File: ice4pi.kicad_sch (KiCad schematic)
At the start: 25 parts, among them J1 Conn_02x03, J2 Raspberry_Pi_2_3, J3 USB_C_Receptacle_USB2.0, J4 RJ45_Amphenol_RJMG1BD3B8K1ANR, U1 ENC28J60x-SS, U2 DSC1001DE1-025.0000

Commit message: feat: poe
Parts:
- removed C1, C2: 100 nF, Capacitor_SMD:C_0402_1005Metric, symbol Device:C
- removed J4: RJ45_Amphenol_RJMG1BD3B8K1ANR, Connector_RJ:RJ45_Amphenol_RJMG1BD3B8K1ANR, symbol Connector:RJ45_Amphenol_RJMG1BD3B8K1ANR
- removed L1: L, Inductor_SMD:L_1210_3225Metric, symbol Device:L
- removed R1, R2, R3, R4: 50, Resistor_SMD:R_0402_1005Metric, symbol Device:R
- removed R6, R7: 1K, Resistor_SMD:R_0402_1005Metric, symbol Device:R
- added C10, C9: 100 nF, Capacitor_SMD:C_0402_1005Metric, symbol Device:C
- added J5: RJ45_Abracon_ARJP11A-MASA-B-A-EMU2, Connector_RJ:RJ45_Abracon_ARJP11A-MA_Horizontal, symbol Connector:RJ45_Abracon_ARJP11A-MASA-B-A-EMU2
- added L2: L, Inductor_SMD:L_1210_3225Metric, symbol Device:L
- added LSI-U1: lsi-powermodule-7, lsi:lsi-powermodule-7, symbol lsi:lsi-powermodule-7
- added R11, R12, R13, R14: 50, Resistor_SMD:R_0402_1005Metric, symbol Device:R
- added R15, R16: 1K, Resistor_SMD:R_0402_1005Metric, symbol Device:R
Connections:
- net +3.3V: now also L2.1
- net +5V: now also LSI-U1.3 (VPP_OUT)
- net GND: now also C10.2, C9.2, J5.12, J5.14, J5.SH, LSI-U1.4 (GND), LSI-U1.5 (S1)
- net LEDA: now also R15.1
- net LEDB: now also R16.1
- new net: C9.1, J5.4 (TCT), L2.2, R11.1, R12.1
- new net: C10.1, J5.5 (RCT), R13.1, R14.1
- new net: J5.6 (RD-), R14.2
- new net: J5.3 (RD+), R13.2
- new net: J5.1 (TD+), R11.2
- new net: J5.11, R15.2
- new net: J5.13, R16.2
- new net: J5.2 (TD-), R12.2
- new net POE_V+: J5.9 (V+), LSI-U1.2 (VPP_IN)
- new net POE_V-: J5.10 (V-), LSI-U1.1 (GND)
- no-connect marks 22 -> 23
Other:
- note removed: "2 to 1 jumper array."
- moved on the sheet: C5, C6, C7, C8, J1, J2, J3, R9

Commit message: feat: commit 2
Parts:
- removed R11, R12, R13, R14: 50, Resistor_SMD:R_0402_1005Metric, symbol Device:R
- added R1, R2, R3, R4: 50, Resistor_SMD:R_0402_1005Metric, symbol Device:R
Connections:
- net TPIN+: now also J5.3 (RD+), R3.2
- net TPIN-: now also J5.6 (RD-), R4.2
- net TPOUT+: now also J5.1 (TD+), R1.2
- net TPOUT-: now also J5.2 (TD-), R2.2
- net at C9.1, J5.4 (TCT), L2.2: now also R1.1, R2.1
- net at C10.1, J5.5 (RCT): now also R3.1, R4.1

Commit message: feat: poe controller
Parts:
- added C15: 100nF 100V, Capacitor_SMD:C_01005_0402Metric, symbol Device:C
- added D4: SMAJ58A, Diode_SMD:D_SMA, symbol Diode:SMAJ58A
- added R22: 24.9K, Resistor_SMD:R_0402_1005Metric, symbol Device:R
- added R23: 180K, Resistor_SMD:R_0402_1005Metric, symbol Device:R
- added R24: 4.42K, Resistor_SMD:R_0402_1005Metric, symbol Device:R
- added U3: TPS2375-1, Package_SO:TSSOP-8_4.4x3mm_P0.65mm, symbol Regulator_Controller:TPS2375-1
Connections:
- net GND: now also LSI-U1.1 (GND), U3.5 (RTN); no longer LSI-U1.5 (S1)
- net POE_V+: now also C15.1, D4.1 (A1), R22.2, U3.8 (VDD)
- net POE_V-: now also C15.2, D4.2 (A2), R23.2, R24.2, U3.4 (VSS); no longer LSI-U1.1 (GND)
- net at LSI-U1.6 (S2): now also U3.6 (PG)
- new net: R22.1, U3.3 (DET)
- new net: R24.1, U3.2 (CLASS)
- new net: R23.1, U3.1 (ILIM)
- no-connect marks 23 -> 26
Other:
- title: ethernet4pizero-1.0 -> ethernet4pizero-poe-1.0
- moved on the sheet: LSI-U1

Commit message: fix: added resistor
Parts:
- added R6: 5.1K, Resistor_SMD:R_0402_1005Metric, symbol Device:R
- C15: footprint Capacitor_SMD:C_01005_0402Metric -> Capacitor_SMD:C_0402_1005Metric
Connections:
- net GND: now also R6.2
- net at J3.B5 (CC2), R9.1: no longer J3.A5 (CC1)
- new net: J3.A5 (CC1), R6.1
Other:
- moved on the sheet: R9
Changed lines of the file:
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@@
 	)
 	(junction
-		(at 50.8 149.86)
+		(at 137.16 45.72)
 		(diameter 0)
 		(color 0 0 0 0)
 	)
 	(junction
-		(at 137.16 45.72)
+		(at 157.48 96.52)
 		(diameter 0)
 		(color 0 0 0 0)
 	)
 	(junction
-		(at 157.48 96.52)
+		(at 39.37 106.68)
 		(diameter 0)
 		(color 0 0 0 0)
 	)
 	(junction
-		(at 39.37 106.68)
+		(at 58.42 149.86)
 		(diameter 0)
 		(color 0 0 0 0)
@@
 	(wire
 		(pts
-			(xy 137.16 43.18) (xy 137.16 45.72)
+			(xy 58.42 149.86) (xy 62.23 149.86)
 		)
 		(stroke
@@
 	(wire
 		(pts
-			(xy 31.75 40.64) (xy 39.37 40.64)
+			(xy 137.16 43.18) (xy 137.16 45.72)
 		)
 		(stroke
@@
 	(wire
 		(pts
-			(xy 71.12 144.78) (xy 76.2 144.78)
+			(xy 31.75 40.64) (xy 39.37 40.64)
 		)
 		(stroke
@@
 	(wire
 		(pts
-			(xy 96.52 106.68) (xy 99.06 106.68)
+			(xy 71.12 144.78) (xy 76.2 144.78)
 		)
 		(stroke
@@
 	(wire
 		(pts
-			(xy 50.8 149.86) (xy 50.8 151.13)
+			(xy 96.52 106.68) (xy 99.06 106.68)
 		)
 		(stroke
@@
 	(wire
 		(pts
-			(xy 50.8 148.59) (xy 50.8 149.86)
-		)
-		(stroke
-			(width 0)
-			(type default)
-		)
-	)
-	(wire
-		(pts
 			(xy 157.48 116.84) (xy 167.64 116.84)
 		)
@@
 	(wire
 		(pts
+			(xy 58.42 149.86) (xy 58.42 151.13)
+		)
+		(stroke
+			(width 0)
+			(type default)
+		)
+	)
+	(wire
+		(pts
 			(xy 96.52 96.52) (xy 99.06 96.52)
 		)
@@
 	(wire
 		(pts
-			(xy 167.64 106.68) (xy 167.64 111.76)
+			(xy 58.42 148.59) (xy 58.42 149.86)
 		)
 		(stroke
@@
 	(wire
 		(pts
-			(xy 97.79 45.72) (xy 101.6 45.72)
+			(xy 167.64 106.68) (xy 167.64 111.76)
 		)
 		(stroke
@@
 	(wire
 		(pts
-			(xy 167.64 96.52) (xy 185.42 96.52)
+			(xy 97.79 45.72) (xy 101.6 45.72)
 		)
 		(stroke
@@
 	(wire
 		(pts
-			(xy 31.75 106.68) (xy 31.75 113.03)
+			(xy 167.64 96.52) (xy 185.42 96.52)
 		)
 		(stroke
@@
 	(wire
 		(pts
-			(xy 142.24 96.52) (xy 142.24 104.14)
+			(xy 31.75 106.68) (xy 31.75 113.03)
 		)
 		(stroke
@@
 	(wire
 		(pts
-			(xy 50.8 149.86) (xy 54.61 149.86)
+			(xy 142.24 96.52) (xy 142.24 104.14)
 		)
 		(stroke
@@
 			)
 		)
-		(property "Footprint" "Capacitor_SMD:C_01005_0402Metric"
+		(property "Footprint" "Capacitor_SMD:C_0402_1005Metric"
 			(at 158.4452 111.76 0)
 			(effects
@@
 	)
 	(symbol
+		(lib_id "Device:R")
+		(at 54.61 148.59 90)
+		(unit 1)
+		(exclude_from_sim no)
+		(in_bom yes)
+		(on_board yes)
+		(dnp no)
+		(property "Reference" "R6"
+			(at 54.61 146.558 90)
+			(effects
+				(font
+					(size 1.27 1.27)
+				)
+			)
+		)
+		(property "Value" "5.1K"
+			(at 54.864 148.59 90)
+			(effects
+				(font
+					(size 1.27 1.27)
+				)
+			)
+		)
+		(property "Footprint" "Resistor_SMD:R_0402_1005Metric"
+			(at 54.61 150.368 90)
+			(effects
+				(font
+					(size 1.27 1.27)
+				)
+				(hide yes)
+			)
+		)
+		(property "Datasheet" "~"
+			(at 54.61 148.59 0)
+			(effects
+				(font
+					(size 1.27 1.27)
+				)
+				(hide yes)
+			)
+		)
+		(property "Description" ""
+			(at 54.61 148.59 0)
+			(effects
+				(font
+					(size 1.27 1.27)
+				)
+				(hide yes)
+			)
+		)
+		(pin "1"
+		)
+		(pin "2"
+		)
+		(instances
+			(project "ice4pi"
+				(path "/0f54db53-a272-4955-88fb-d7ab00657bb0"
+					(reference "R6")
+					(unit 1)
+				)
+			)
+		)
+	)
+	(symbol
 		(lib_id "power:+3.3V")
 		(at 24.13 91.44 0)
@@
 	(symbol
 		(lib_id "Device:R")
-		(at 54.61 153.67 0)
+		(at 54.61 151.13 90)
 		(unit 1)
 		(exclude_from_sim no)
@@
 		(on_board yes)
 		(dnp no)
-		(fields_autoplaced yes)
 		(property "Reference" "R9"
-			(at 57.15 152.3999 0)
+			(at 54.61 151.13 90)
 			(effects
 				(font
 					(size 1.27 1.27)
 				)
-				(justify left)
 			)
 		)
 		(property "Value" "5.1K"
-			(at 57.15 154.9399 0)
+			(at 54.61 152.908 90)
 			(effects
 				(font
 					(size 1.27 1.27)
 				)
-				(justify left)
 			)
 		)
 		(property "Footprint" "Resistor_SMD:R_0402_1005Metric"
-			(at 52.832 153.67 90)
+			(at 54.61 152.908 90)
 			(effects
 				(font
@@
 		)
 		(property "Datasheet" "~"
-			(at 54.61 153.67 0)
+			(at 54.61 151.13 0)
 			(effects
 				(font
@@
 		)
 		(property "Description" ""
-			(at 54.61 153.67 0)
+			(at 54.61 151.13 0)
 			(effects
 				(font
@@
 	(symbol
 		(lib_id "power:GND")
-		(at 54.61 157.48 0)
+		(at 62.23 149.86 0)
 		(unit 1)
 		(exclude_from_sim no)
@@
 		(fields_autoplaced yes)
 		(property "Reference" "#PWR0112"
-			(at 54.61 163.83 0)
+			(at 62.23 156.21 0)
 			(effects
 				(font
@@
 		)
 		(property "Value" "GND"
-			(at 54.61 162.56 0)
+			(at 62.23 154.94 0)
 			(effects
 				(font
@@
 		)
 		(property "Footprint" ""
-			(at 54.61 157.48 0)
+			(at 62.23 149.86 0)
 			(effects
 				(font
@@
 		)
 		(property "Datasheet" ""
-			(at 54.61 157.48 0)
+			(at 62.23 149.86 0)
 			(effects
 				(font
@@
 		)
 		(property "Description" ""
-			(at 54.61 157.48 0)
+			(at 62.23 149.86 0)
 			(effects
 				(font

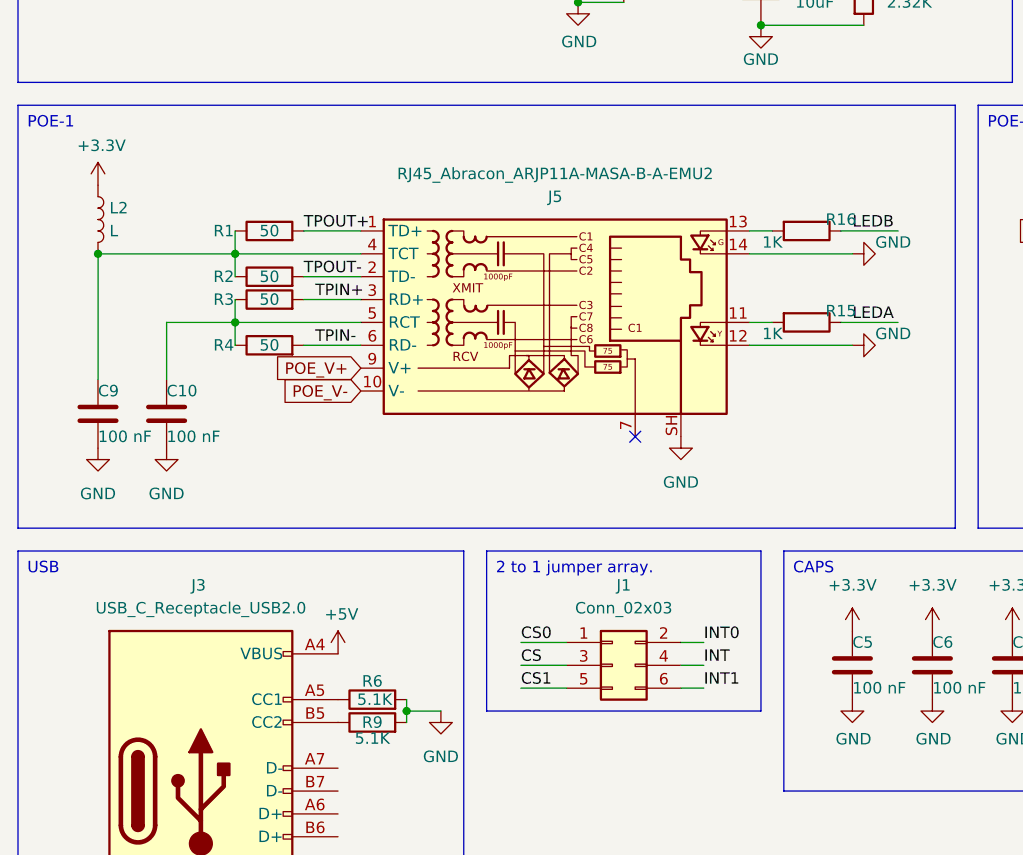
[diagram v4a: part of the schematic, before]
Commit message: feat: pos.csv
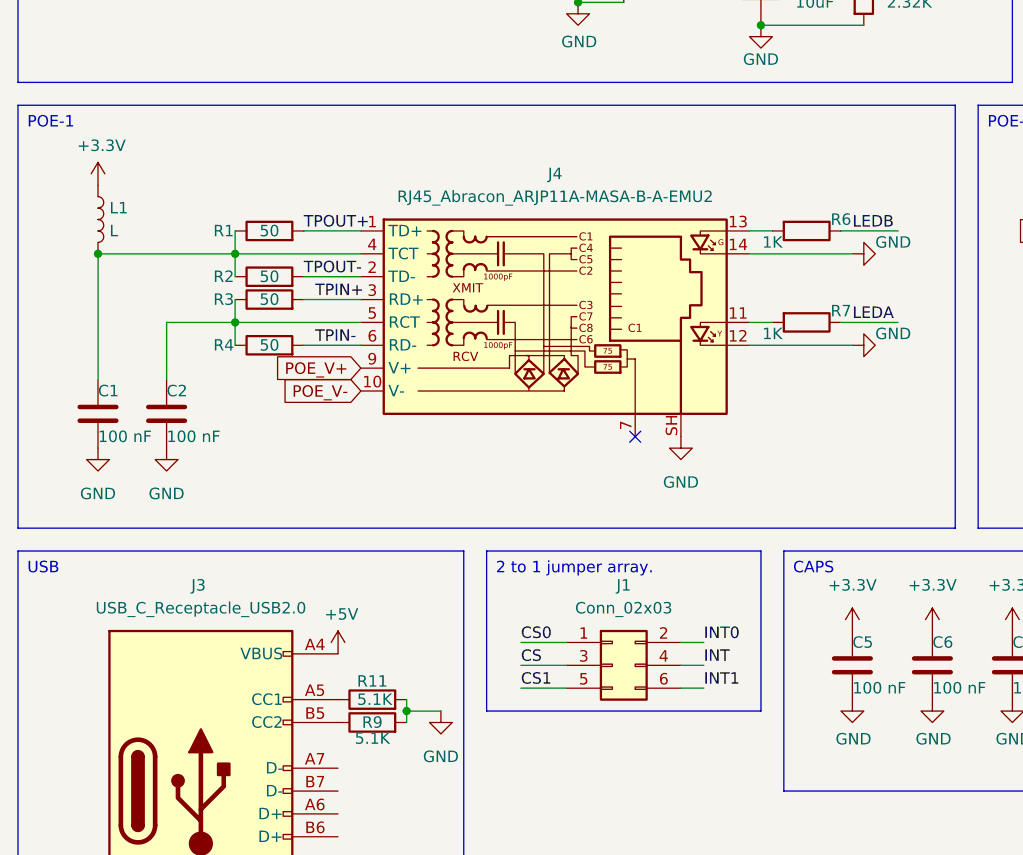
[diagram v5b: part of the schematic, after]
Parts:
- renumbered C9 to C1, C10 to C2, J5 to J4, L2 to L1, R6 to R11, R16 to R6, R15 to R7
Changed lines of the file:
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@@
 		(on_board yes)
 		(dnp no)
-		(property "Reference" "R6"
+		(property "Reference" "R11"
 			(at 54.61 146.558 90)
 			(effects
@@
 			(project "ice4pi"
 				(path "/0f54db53-a272-4955-88fb-d7ab00657bb0"
-					(reference "R6")
+					(reference "R11")
 					(unit 1)
 				)
@@
 		(on_board yes)
 		(dnp no)
-		(property "Reference" "C9"
+		(property "Reference" "C1"
 			(at 24.13 114.3 0)
 			(effects
@@
 			(project "ice4pi"
 				(path "/0f54db53-a272-4955-88fb-d7ab00657bb0"
-					(reference "C9")
+					(reference "C1")
 					(unit 1)
 				)
@@
 		(on_board yes)
 		(dnp no)
-		(property "Reference" "C10"
+		(property "Reference" "C2"
 			(at 31.75 114.3 0)
 			(effects
@@
 			(project "ice4pi"
 				(path "/0f54db53-a272-4955-88fb-d7ab00657bb0"
-					(reference "C10")
+					(reference "C2")
 					(unit 1)
 				)
@@
 		(dnp no)
 		(fields_autoplaced yes)
-		(property "Reference" "L2"
+		(property "Reference" "L1"
 			(at 25.4 93.9799 0)
 			(effects
@@
 			(project "ice4pi"
 				(path "/0f54db53-a272-4955-88fb-d7ab00657bb0"
-					(reference "L2")
+					(reference "L1")
 					(unit 1)
 				)
@@
 		(dnp no)
 		(fields_autoplaced yes)
-		(property "Reference" "J5"
-			(at 74.93 92.71 0)
+		(property "Reference" "J4"
+			(at 74.93 90.17 0)
 			(effects
 				(font
@@
 		)
 		(property "Value" "RJ45_Abracon_ARJP11A-MASA-B-A-EMU2"
-			(at 74.93 90.17 0)
+			(at 74.93 92.71 0)
 			(effects
 				(font
@@
 			(project ""
 				(path "/0f54db53-a272-4955-88fb-d7ab00657bb0"
-					(reference "J5")
+					(reference "J4")
 					(unit 1)
 				)
@@
 		(on_board yes)
 		(dnp no)
-		(property "Reference" "R15"
+		(property "Reference" "R7"
 			(at 106.68 105.41 90)
 			(effects
@@
 			(project "ice4pi"
 				(path "/0f54db53-a272-4955-88fb-d7ab00657bb0"
-					(reference "R15")
+					(reference "R7")
 					(unit 1)
 				)
@@
 		(on_board yes)
 		(dnp no)
-		(property "Reference" "R16"
+		(property "Reference" "R6"
 			(at 106.68 95.25 90)
 			(effects
@@
 			(project "ice4pi"
 				(path "/0f54db53-a272-4955-88fb-d7ab00657bb0"
-					(reference "R16")
+					(reference "R6")
 					(unit 1)
 				)
